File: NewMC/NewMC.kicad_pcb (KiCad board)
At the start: 4 copper layers, 4 parts, among them J1 Conn_01x09_Pin, M1 Motor_DC, M2 Motor_DC, U1 TB6612FNG

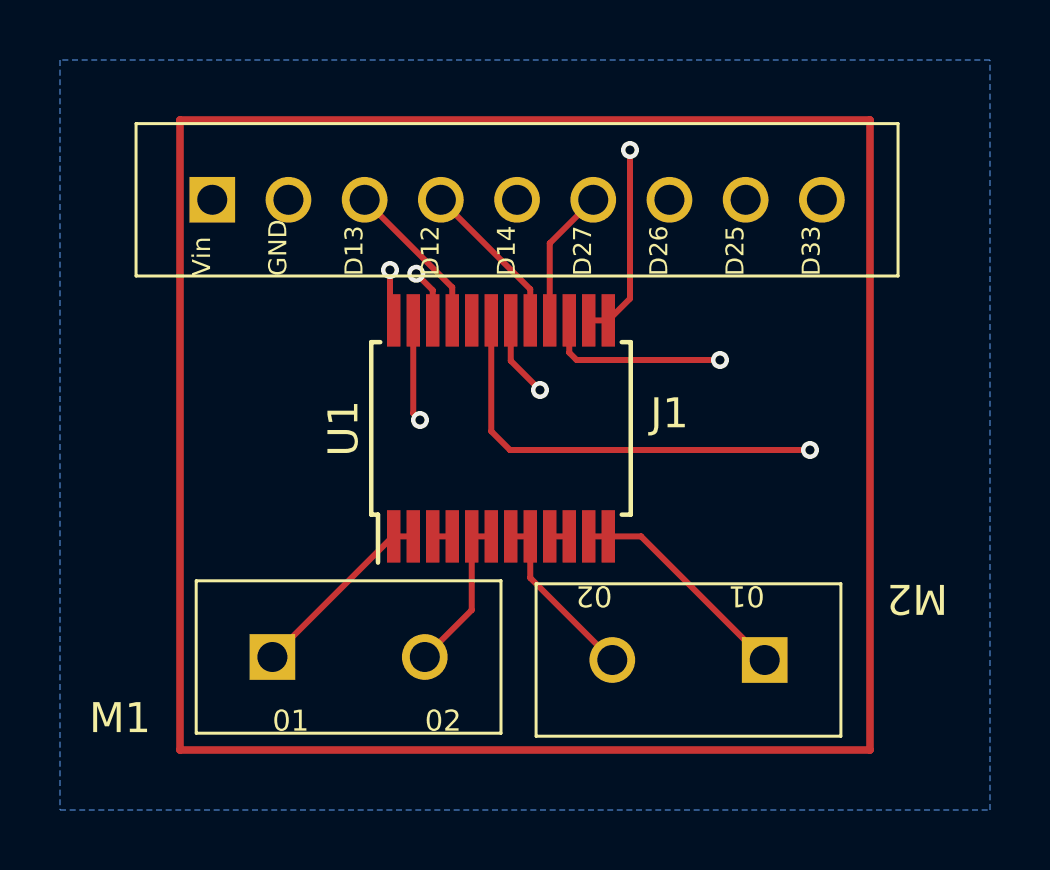
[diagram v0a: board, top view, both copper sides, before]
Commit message: Add files via upload
This file include the schematics of the connection between ESP32 and TB6612FNG motor controller see NewMCwESP
the PCB design for the board carrying TB6612FNG is also included
For pcb design, JLCPCB 1-2 layer is used
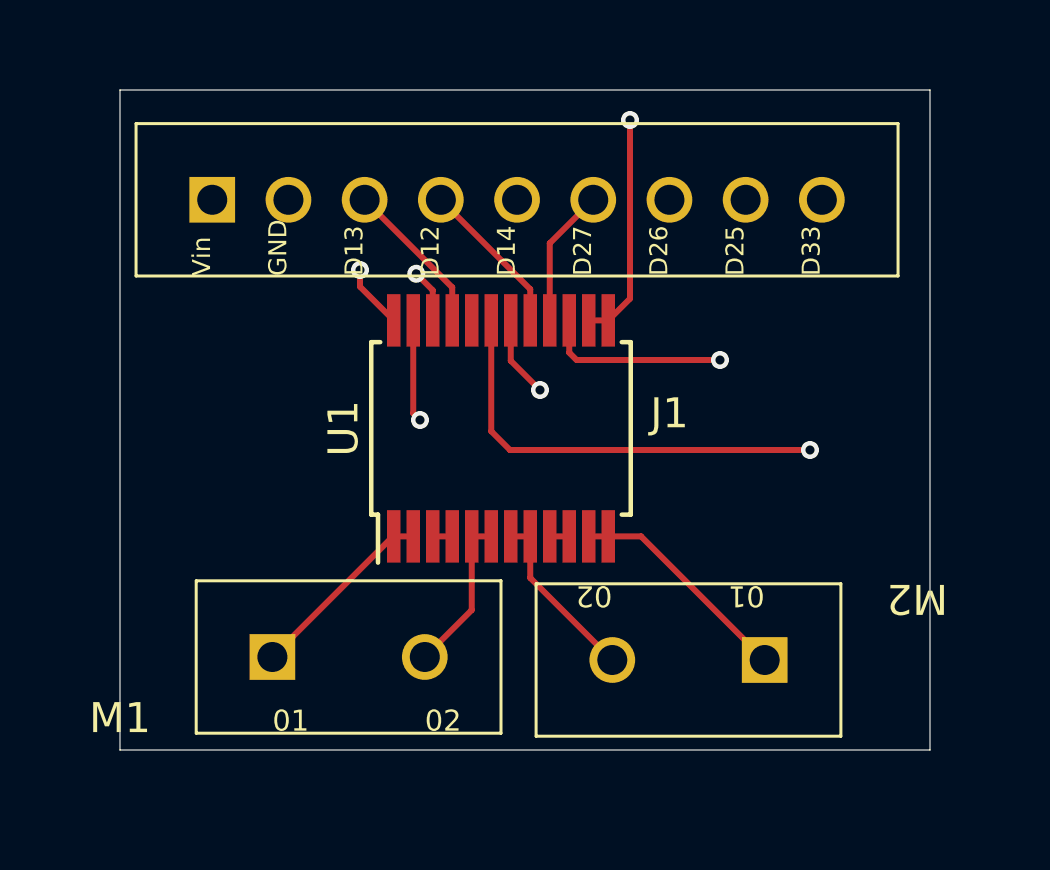
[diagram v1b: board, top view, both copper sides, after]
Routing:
- net +5V: track 27.6 -> 29.8 mm
- removed copper zone on B.Cu, net GND
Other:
- board outline added: 27 x 22 mm
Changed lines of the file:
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@@
     )
   )
-  (gr_line (start 152 92) (end 152 71)
-    (stroke (width 0.254) (type default)) (layer "F.Cu"))
-  (gr_line (start 129 92) (end 152 92)
-    (stroke (width 0.254) (type default)) (layer "F.Cu"))
-  (gr_line (start 129 71) (end 129 92)
-    (stroke (width 0.254) (type default)) (layer "F.Cu"))
-  (gr_line (start 152 71) (end 129 71)
-    (stroke (width 0.254) (type default)) (layer "F.Cu"))
+  (gr_line (start 154 92) (end 154 70)
+    (stroke (width 0.0381) (type default)) (layer "Edge.Cuts"))
+  (gr_line (start 127 92) (end 154 92)
+    (stroke (width 0.0381) (type default)) (layer "Edge.Cuts"))
+  (gr_line (start 154 70) (end 127 70)
+    (stroke (width 0.0381) (type default)) (layer "Edge.Cuts"))
+  (gr_line (start 127 70) (end 127 92)
+    (stroke (width 0.0381) (type default)) (layer "Edge.Cuts"))
+  (segment (start 144 76.955) (end 143.275 77.68) (width 0.2) (layer "F.Cu") (net 1))
   (segment (start 143.275 77.68) (end 142.625 77.68) (width 0.2) (layer "F.Cu") (net 1))
-  (segment (start 136 76) (end 136 77.555) (width 0.2) (layer "F.Cu") (net 1))
-  (segment (start 136 77.555) (end 136.125 77.68) (width 0.2) (layer "F.Cu") (net 1))
-  (segment (start 144 76.955) (end 143.275 77.68) (width 0.2) (layer "F.Cu") (net 1))
-  (segment (start 144 72) (end 144 76.955) (width 0.2) (layer "F.Cu") (net 1))
-  (via (at 144 72) (size 0.6) (drill 0.3) (layers "F.Cu" "B.Cu") (net 1))
-  (via (at 136 76) (size 0.6) (drill 0.3) (layers "F.Cu" "B.Cu") (net 1))
-  (segment (start 136.706 72.706) (end 136.706 75.294) (width 0.2) (layer "In1.Cu") (net 1))
+  (segment (start 135 76.555) (end 136.125 77.68) (width 0.2) (layer "F.Cu") (net 1))
+  (segment (start 144 71) (end 144 76.955) (width 0.2) (layer "F.Cu") (net 1))
+  (segment (start 135 76) (end 135 76.555) (width 0.2) (layer "F.Cu") (net 1))
+  (via (at 144 71) (size 0.6) (drill 0.3) (layers "F.Cu" "B.Cu") (net 1))
+  (via (at 135 76) (size 0.6) (drill 0.3) (layers "F.Cu" "B.Cu") (net 1))
   (segment (start 130.075 73.66) (end 131.735 72) (width 0.2) (layer "In1.Cu") (net 1))
-  (segment (start 136 72) (end 136.706 72.706) (width 0.2) (layer "In1.Cu") (net 1))
+  (segment (start 135 76) (end 136.706 74.294) (width 0.2) (layer "In1.Cu") (net 1))
+  (segment (start 143 72) (end 144 71) (width 0.2) (layer "In1.Cu") (net 1))
   (segment (start 131.735 72) (end 136 72) (width 0.2) (layer "In1.Cu") (net 1))
-  (segment (start 136 72) (end 144 72) (width 0.2) (layer "In1.Cu") (net 1))
-  (segment (start 136.706 75.294) (end 136 76) (width 0.2) (layer "In1.Cu") (net 1))
+  (segment (start 136.706 74.294) (end 136.706 72.706) (width 0.2) (layer "In1.Cu") (net 1))
+  (segment (start 136.706 72.706) (end 136 72) (width 0.2) (layer "In1.Cu") (net 1))
+  (segment (start 136 72) (end 143 72) (width 0.2) (layer "In1.Cu") (net 1))
   (segment (start 141 80) (end 140.025 79.025) (width 0.2) (layer "F.Cu") (net 2))
   (segment (start 140.025 79.025) (end 140.025 77.68) (width 0.2) (layer "F.Cu") (net 2))
@@
   (segment (start 137.425 84.88) (end 138.075 84.88) (width 0.2) (layer "F.Cu") (net 14))
   (segment (start 141.975 84.88) (end 141.325 84.88) (width 0.2) (layer "F.Cu") (net 15))
-  (zone (net 2) (net_name "GND") (layer "B.Cu") (hatch edge 0.5)
-    (connect_pads (clearance 0.5))
-    (min_thickness 0.25) (filled_areas_thickness no)
-    (fill (thermal_gap 0.5) (thermal_bridge_width 0.5))
-    (polygon
-      (pts
-        (xy 125 94)
-        (xy 156 94)
-        (xy 156 69)
-        (xy 125 69)
-      )
-    )
-  )
 )
